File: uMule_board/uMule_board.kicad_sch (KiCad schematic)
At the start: 0 parts

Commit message: added notes for development
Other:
- added sheet Photodiode (sheets/photodiode.kicad_sch)
- sheet Power ports: added +3V3, +5V, SCL, SDA, VBUS, VCC, VSUP+, VSUP-; removed none
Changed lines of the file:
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@@
 	(paper "A4")
 	(sheet
-		(at 25.4 22.86)
-		(size 25.4 17.78)
+		(at 182.88 34.29)
+		(size 20.32 15.24)
+		(exclude_from_sim no)
+		(in_bom yes)
+		(on_board yes)
+		(dnp no)
+		(fields_autoplaced yes)
+		(stroke
+			(width 0.1524)
+			(type solid)
+		)
+		(fill
+			(color 0 0 0 0.0000)
+		)
+		(property "Sheetname" "Photodiode"
+			(at 182.88 33.5784 0)
+			(effects
+				(font
+					(size 1.27 1.27)
+				)
+				(justify left bottom)
+			)
+		)
+		(property "Sheetfile" "sheets/photodiode.kicad_sch"
+			(at 182.88 50.1146 0)
+			(effects
+				(font
+					(size 1.27 1.27)
+				)
+				(justify left top)
+			)
+		)
+		(instances
+			(project "uMule_board"
+				(path "/3d853824-a92e-40a5-ad1a-5052c8a0bd68"
+					(page "4")
+				)
+			)
+		)
+	)
+	(sheet
+		(at 39.37 30.48)
+		(size 31.75 21.59)
 		(exclude_from_sim no)
 		(in_bom yes)
@@
 		)
 		(property "Sheetname" "Power"
-			(at 25.4 22.1484 0)
+			(at 39.37 29.7684 0)
 			(effects
 				(font
@@
 		)
 		(property "Sheetfile" "sheets/power.kicad_sch"
-			(at 25.4 41.2246 0)
+			(at 39.37 52.6546 0)
 			(effects
 				(font
@@
 				)
 				(justify left top)
+			)
+		)
+		(pin "+3V3" output
+			(at 71.12 40.64 0)
+			(effects
+				(font
+					(size 1.27 1.27)
+				)
+				(justify right)
+			)
+		)
+		(pin "+5V" output
+			(at 71.12 38.1 0)
+			(effects
+				(font
+					(size 1.27 1.27)
+				)
+				(justify right)
+			)
+		)
+		(pin "SCL" input
+			(at 71.12 49.53 0)
+			(effects
+				(font
+					(size 1.27 1.27)
+				)
+				(justify right)
+			)
+		)
+		(pin "SDA" bidirectional
+			(at 71.12 46.99 0)
+			(effects
+				(font
+					(size 1.27 1.27)
+				)
+				(justify right)
+			)
+		)
+		(pin "VBUS" input
+			(at 39.37 39.37 180)
+			(effects
+				(font
+					(size 1.27 1.27)
+				)
+				(justify left)
+			)
+		)
+		(pin "VCC" output
+			(at 71.12 35.56 0)
+			(effects
+				(font
+					(size 1.27 1.27)
+				)
+				(justify right)
+			)
+		)
+		(pin "VSUP+" input
+			(at 39.37 35.56 180)
+			(effects
+				(font
+					(size 1.27 1.27)
+				)
+				(justify left)
+			)
+		)
+		(pin "VSUP-" input
+			(at 39.37 49.53 180)
+			(effects
+				(font
+					(size 1.27 1.27)
+				)
+				(justify left)
 			)
 		)
@@
 	)
 	(sheet
-		(at 68.58 24.13)
-		(size 38.1 21.59)
+		(at 109.22 30.48)
+		(size 38.1 54.61)
 		(exclude_from_sim no)
 		(in_bom yes)
@@
 		)
 		(property "Sheetname" "MCU"
-			(at 68.58 23.4184 0)
+			(at 109.22 29.7684 0)
 			(effects
 				(font
@@
 		)
 		(property "Sheetfile" "sheets/mcu.kicad_sch"
-			(at 68.58 46.3046 0)
+			(at 109.22 85.6746 0)
 			(effects
 				(font

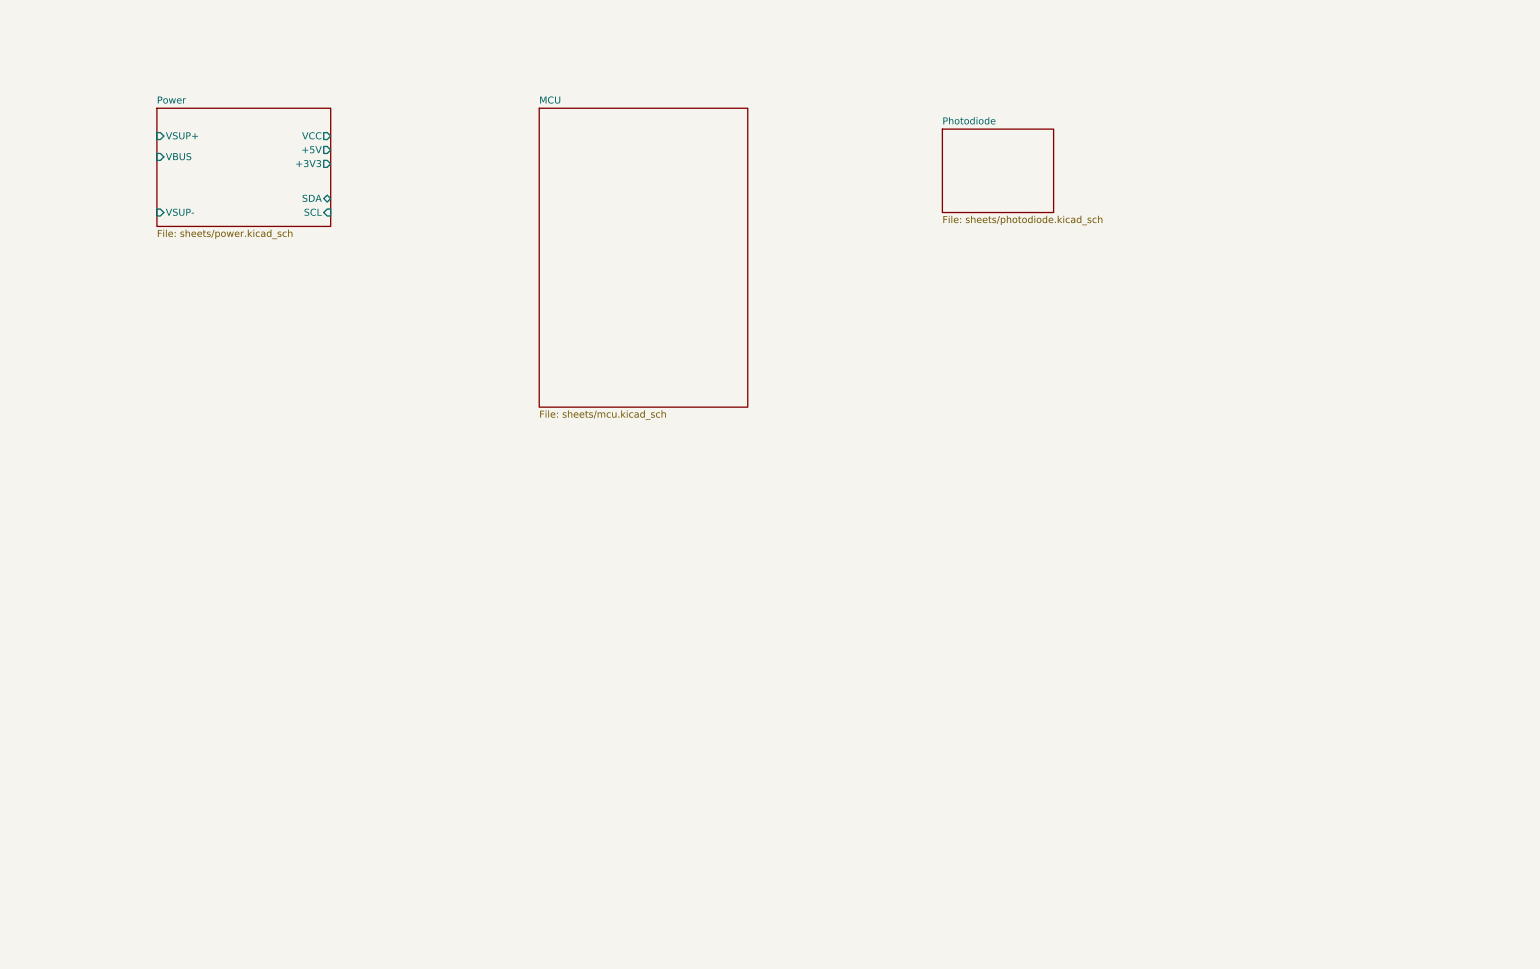
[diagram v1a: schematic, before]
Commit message: addd buses and simple connections
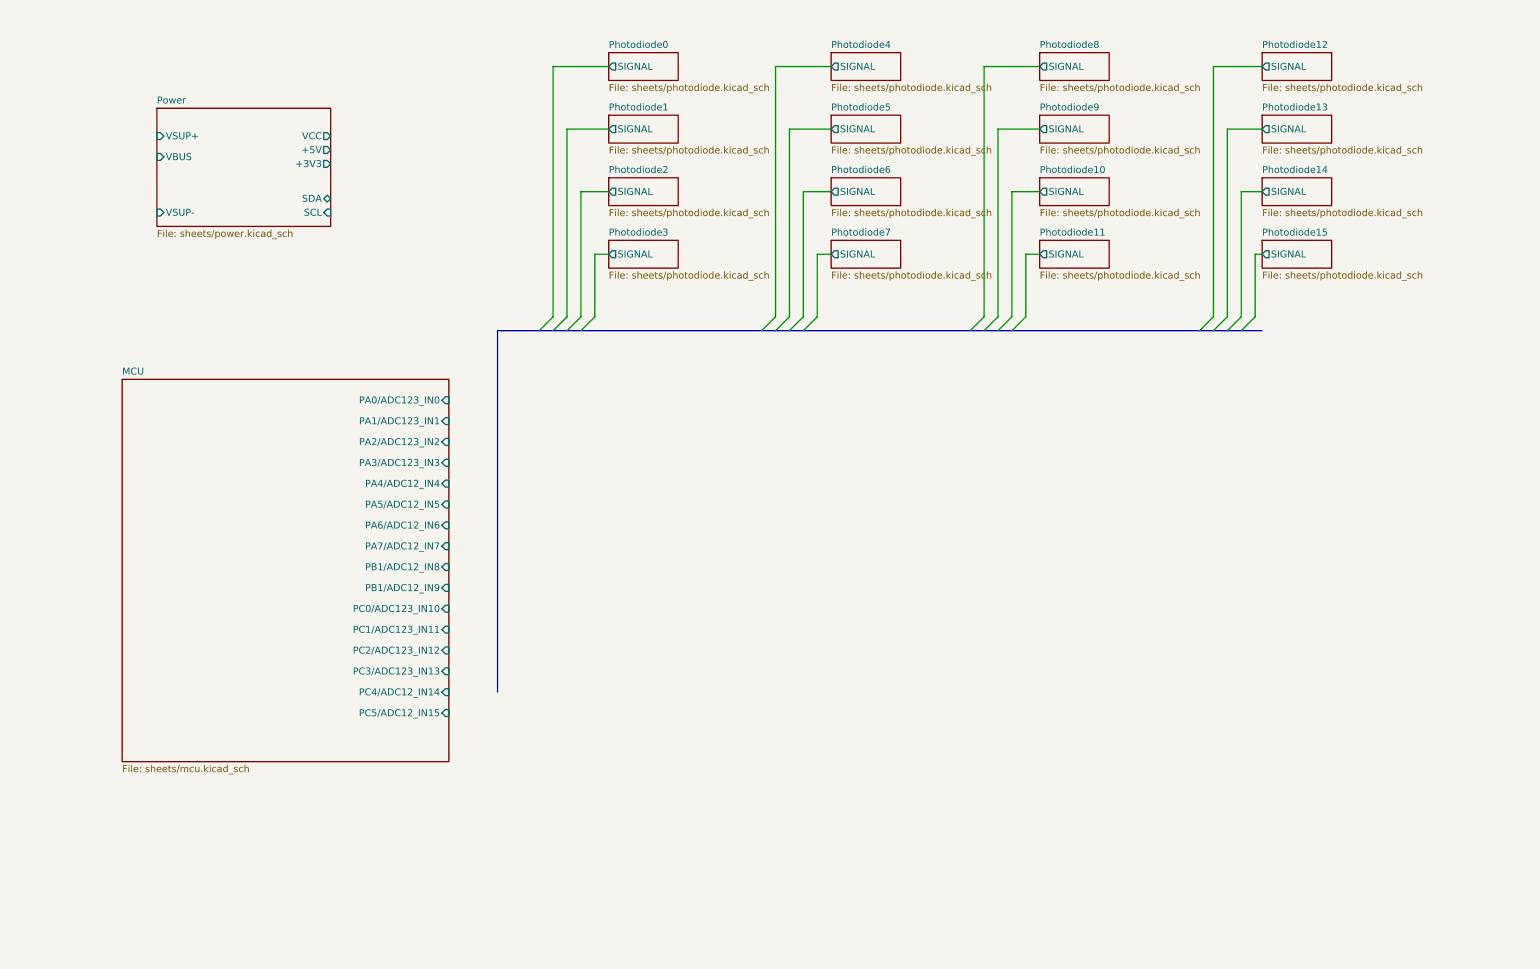
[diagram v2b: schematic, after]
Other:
- sheet Photodiode renamed Photodiode0
- added sheet Photodiode1 (sheets/photodiode.kicad_sch)
- added sheet Photodiode10 (sheets/photodiode.kicad_sch)
- added sheet Photodiode11 (sheets/photodiode.kicad_sch)
- added sheet Photodiode12 (sheets/photodiode.kicad_sch)
- added sheet Photodiode13 (sheets/photodiode.kicad_sch)
- added sheet Photodiode14 (sheets/photodiode.kicad_sch)
- added sheet Photodiode15 (sheets/photodiode.kicad_sch)
- added sheet Photodiode2 (sheets/photodiode.kicad_sch)
- added sheet Photodiode3 (sheets/photodiode.kicad_sch)
- added sheet Photodiode4 (sheets/photodiode.kicad_sch)
- added sheet Photodiode5 (sheets/photodiode.kicad_sch)
- added sheet Photodiode6 (sheets/photodiode.kicad_sch)
- added sheet Photodiode7 (sheets/photodiode.kicad_sch)
- added sheet Photodiode8 (sheets/photodiode.kicad_sch)
- added sheet Photodiode9 (sheets/photodiode.kicad_sch)
- sheet MCU ports: added PA0/ADC123_IN0, PA1/ADC123_IN1, PA2/ADC123_IN2, PA3/ADC123_IN3, PA4/ADC12_IN4, PA5/ADC12_IN5, PA6/ADC12_IN6, PA7/ADC12_IN7, PB1/ADC12_IN8, PB1/ADC12_IN9, PC0/ADC123_IN10, PC1/ADC123_IN11, PC2/ADC123_IN12, PC3/ADC123_IN13, PC4/ADC12_IN14, PC5/ADC12_IN15; removed none
- sheet Photodiode0 ports: added SIGNAL; removed none

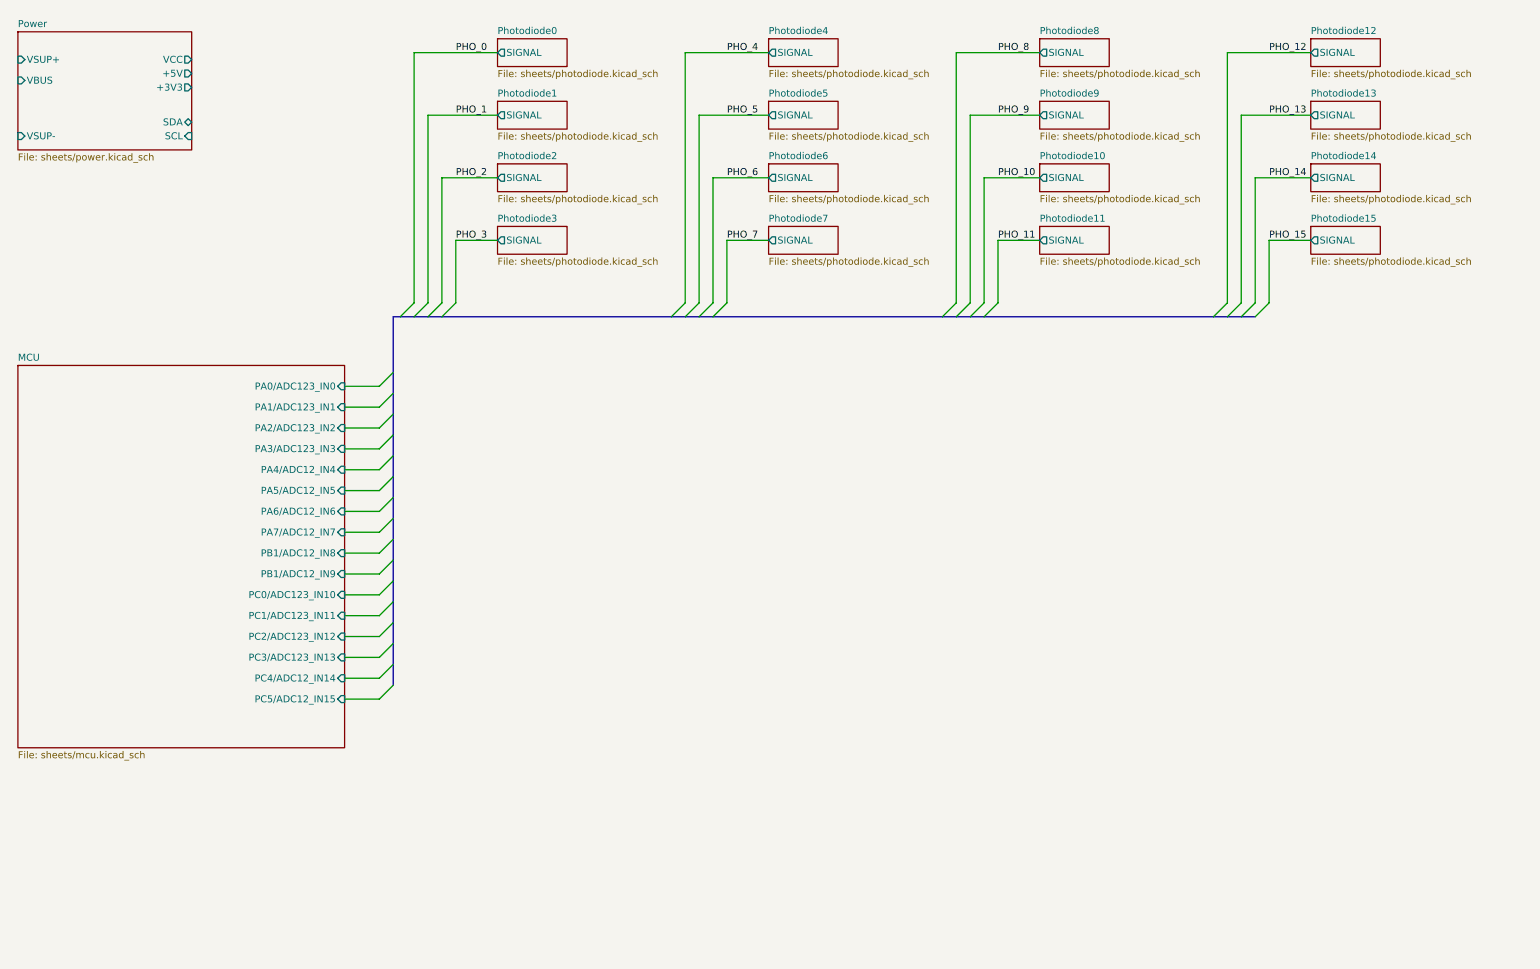
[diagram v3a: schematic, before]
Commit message: all main componenst added. Prepared to change MCU. SCH almost ready
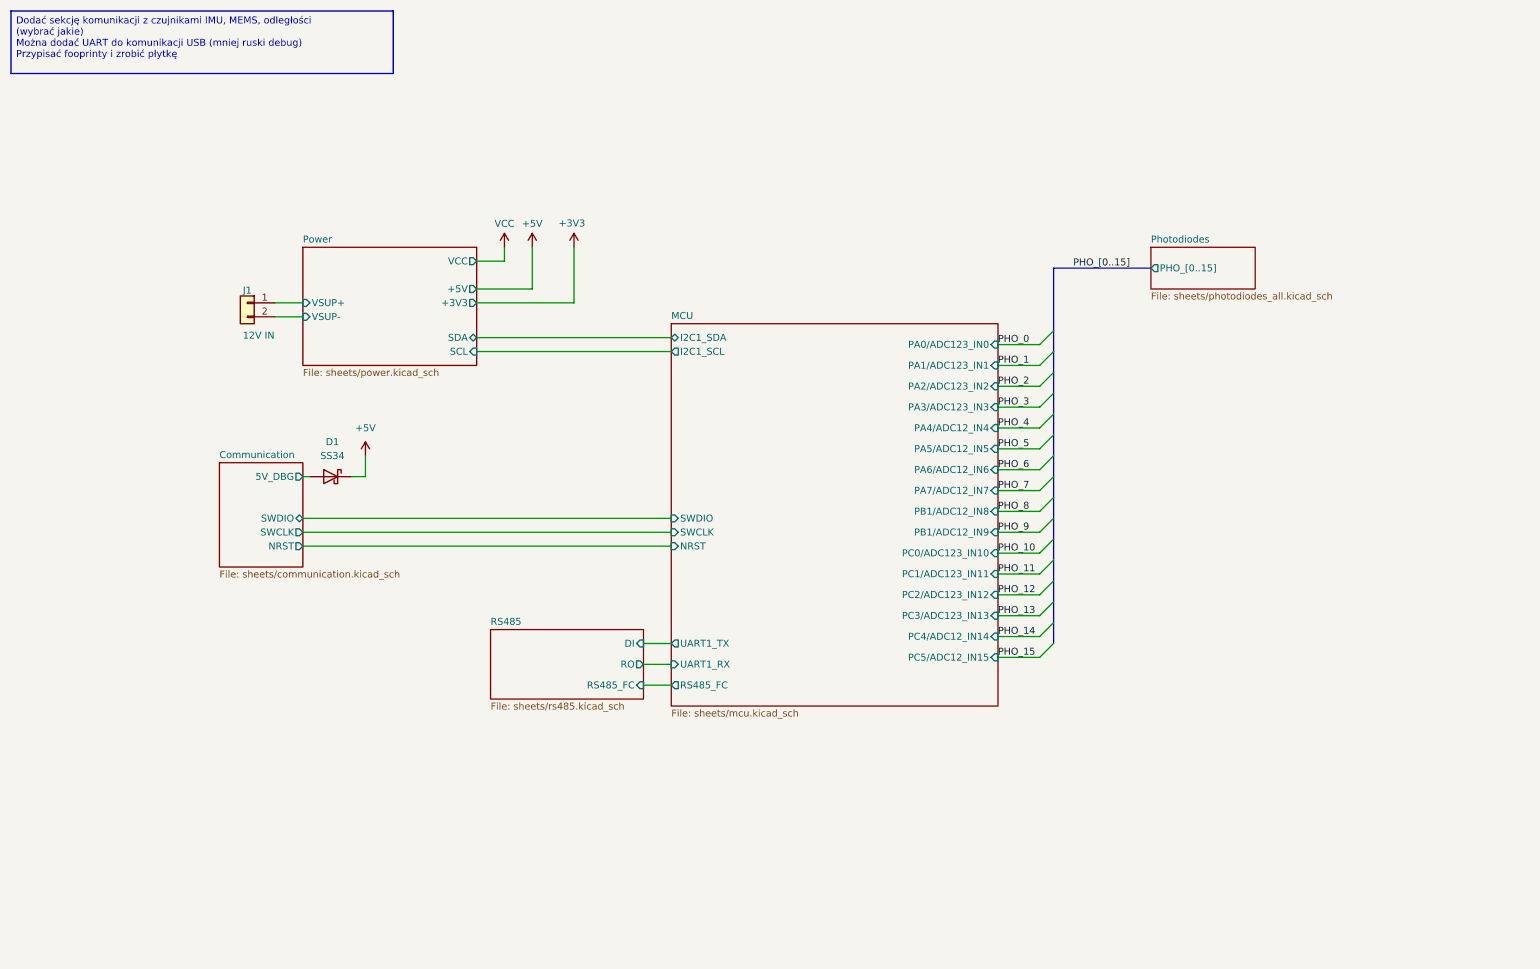
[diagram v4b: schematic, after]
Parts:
- added D1: SS34, Diode_SMD:D_SMA, symbol Diode:SS34
- added J1: 12V IN, Connector_Phoenix_MC:PhoenixContact_MC_1,5_2-G-3.5_1x02_P3.50mm_Horizontal, symbol Connector_Generic:Conn_01x02
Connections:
- net Power/VSUP+: now also J1.1 (Pin_1)
- net Power/VSUP-: now also J1.2 (Pin_2)
- new net +5V: D1.1 (K)
- new net Communication/5V_DBG: D1.2 (A)
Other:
- removed sheet Photodiode0
- removed sheet Photodiode1
- removed sheet Photodiode10
- removed sheet Photodiode11
- removed sheet Photodiode12
- removed sheet Photodiode13
- removed sheet Photodiode14
- removed sheet Photodiode15
- removed sheet Photodiode2
- removed sheet Photodiode3
- removed sheet Photodiode4
- removed sheet Photodiode5
- removed sheet Photodiode6
- removed sheet Photodiode7
- removed sheet Photodiode8
- removed sheet Photodiode9
- added sheet Communication (sheets/communication.kicad_sch)
- added sheet Photodiodes (sheets/photodiodes_all.kicad_sch)
- added sheet RS485 (sheets/rs485.kicad_sch)
- sheet MCU ports: added I2C1_SCL, I2C1_SDA, NRST, RS485_FC, SWCLK, SWDIO, UART1_RX, UART1_TX; removed none
- sheet Power ports: added none; removed VBUS

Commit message: Finished schematics. Now ready for PCB
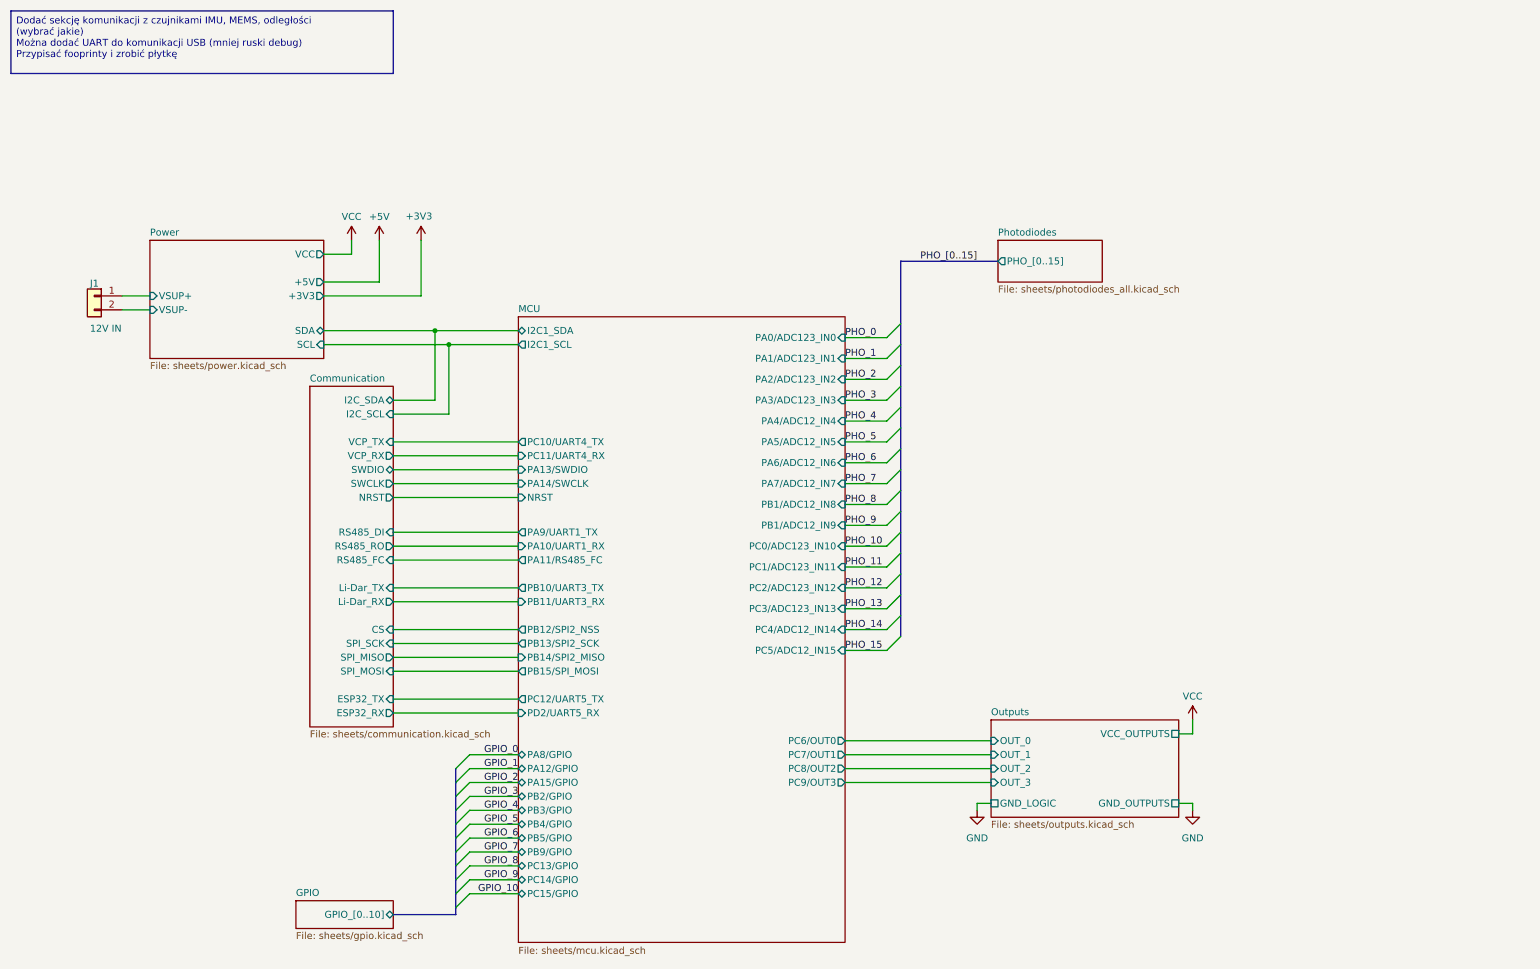
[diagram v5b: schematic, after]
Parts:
- removed D1: SS34, Diode_SMD:D_SMA, symbol Diode:SS34
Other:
- removed sheet RS485
- added sheet GPIO (sheets/gpio.kicad_sch)
- added sheet Outputs (sheets/outputs.kicad_sch)
- sheet Communication ports: added CS, ESP32_RX, ESP32_TX, I2C_SCL, I2C_SDA, Li-Dar_RX, Li-Dar_TX, RS485_DI, RS485_FC, RS485_RO, SPI_MISO, SPI_MOSI, SPI_SCK, VCP_RX, VCP_TX; removed 5V_DBG
- sheet MCU ports: added PA10/UART1_RX, PA11/RS485_FC, PA12/GPIO, PA13/SWDIO, PA14/SWCLK, PA15/GPIO, PA8/GPIO, PA9/UART1_TX, PB10/UART3_TX, PB11/UART3_RX, PB12/SPI2_NSS, PB13/SPI2_SCK, PB14/SPI2_MISO, PB15/SPI_MOSI, PB2/GPIO, PB3/GPIO, PB4/GPIO, PB5/GPIO, PB9/GPIO, PC10/UART4_TX, PC11/UART4_RX, PC12/UART5_TX, PC13/GPIO, PC14/GPIO, PC15/GPIO, PC6/OUT0, PC7/OUT1, PC8/OUT2, PC9/OUT3, PD2/UART5_RX; removed RS485_FC, SWCLK, SWDIO, UART1_RX, UART1_TX
- moved on the sheet: J1
